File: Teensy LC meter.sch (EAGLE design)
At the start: 20 parts, among them J1 TEENSY-LC, T1 2N2222, T2 2N2222, T3 2N2222, T4 2N2222, U1 CD4543

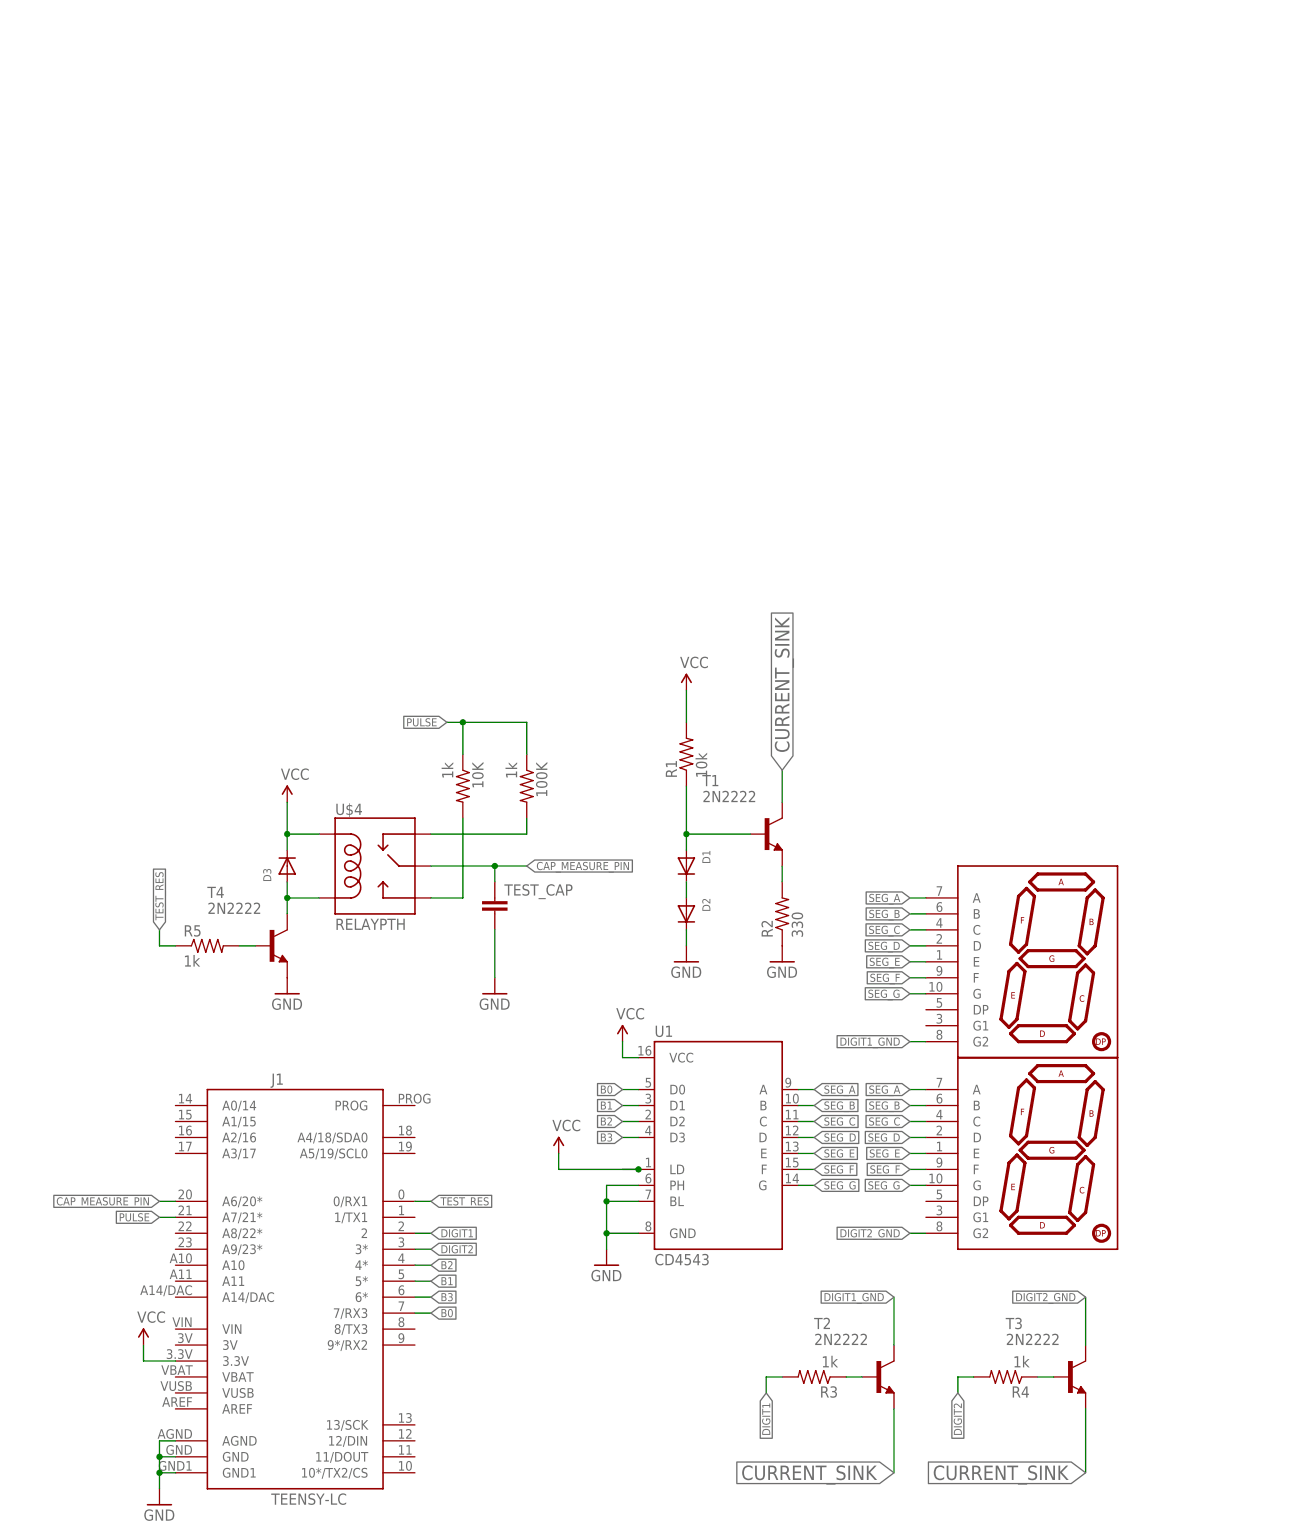
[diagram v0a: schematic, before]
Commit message: Improvements regarding measurements. * Using CLK counts instead of micros() for the time measurements. * Started to add code for inductance meter. Haven't tested yet. * Updated Schematic
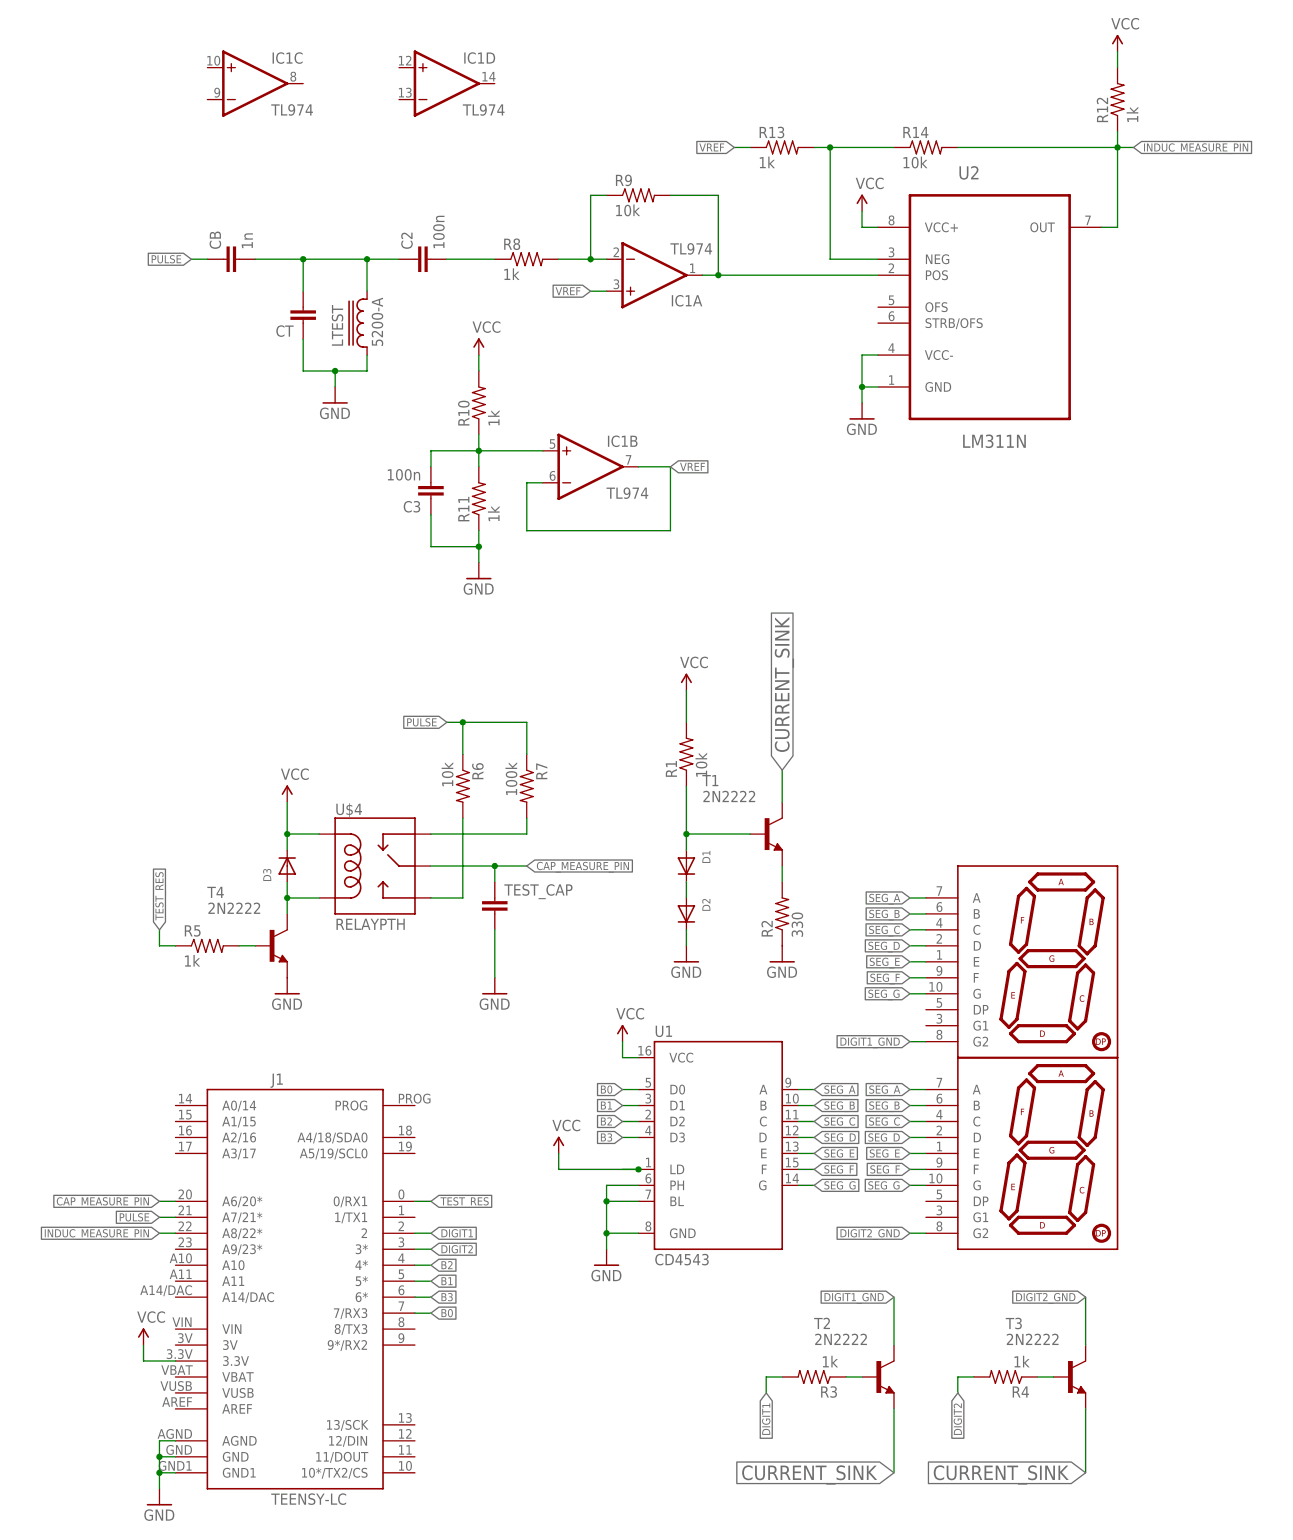
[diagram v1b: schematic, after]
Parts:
- added C2, C3: 100n, SparkFun-Capacitors:CAPPTH
- added CB: 1n, SparkFun-Capacitors:CAPPTH
- added CT: (no value), SparkFun-Capacitors:CAPPTH
- added IC1: TL974, adafruit:QUAD_OPAMPD
- added LTEST: 5200-A, Bounrs-Ind:5200-A
- added R10, R11, R12, R13, R8: 1k, adafruit:FLIPFLOP-RES
- added R14, R9: 10k, adafruit:FLIPFLOP-RES
- added U2: LM311N, ST Microelctronics_By_element14_Batch_1:LM311N
- R6: value 1k -> 10k
- R7: value 1k -> 100k
- renumbered 100K to R7, 10K to R6
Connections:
- new net INDUC_MEASURE_PIN: J1.A8/22*, R12.1, R14.2, U2.OUT
- new net N$11: IC1A.OUT, R9.2, U2.POS
- new net N$12: C2.2, R8.1
- new net N$13: C2.1, CB.2, CT.2, LTEST.2
- new net N$14: C3.2, IC1B.+IN, R10.1, R11.2
- new net N$17: R13.2, R14.1, U2.NEG
- new net N$4: IC1A.-IN, R8.2, R9.1
- new net VREF: IC1A.+IN, IC1B.-IN, IC1B.OUT, R13.1
- net GND: now also C3.1, CT.1, LTEST.1, R11.1, U2.GND, U2.VCC-
- net PULSE: now also CB.1
- net VCC: now also R10.2, R12.2, U2.VCC+
